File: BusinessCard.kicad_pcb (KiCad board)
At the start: 2 copper layers, 85.6 x 56 mm, 7 parts, among them U1 NT3H2111W0FHKH

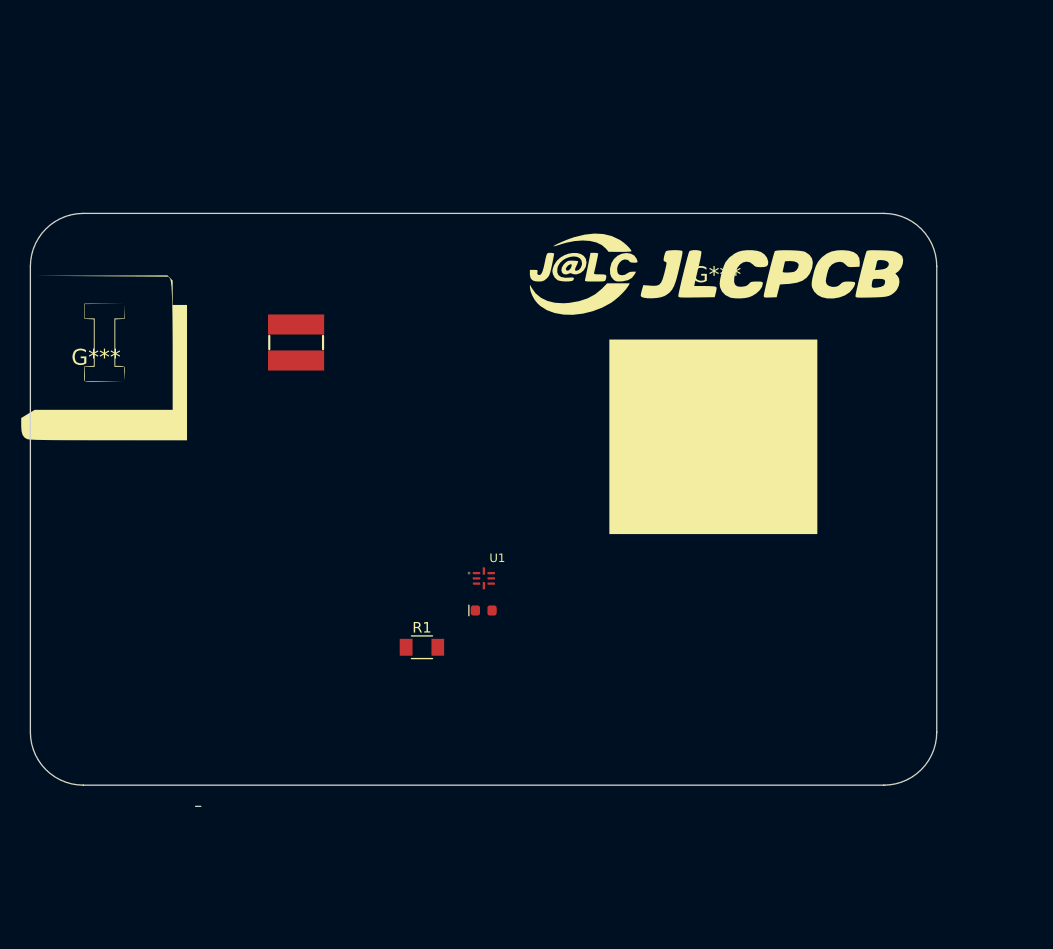
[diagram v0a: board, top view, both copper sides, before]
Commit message: logos added to footprint
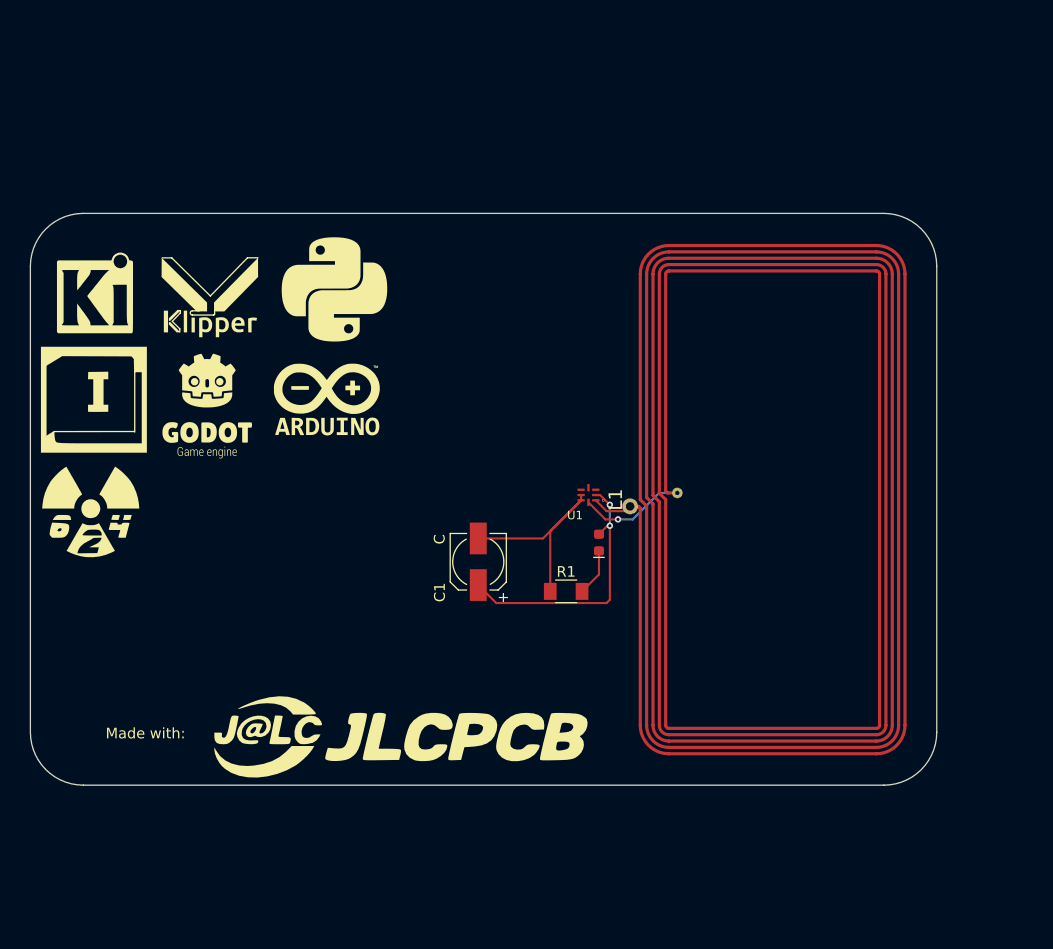
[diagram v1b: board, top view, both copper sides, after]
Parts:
- removed the G*** at (138.4, 87.1)
- added C1: C, PCM_4ms_Capacitor:CP_Elec_5x5.3, F.Cu at (116.2, 98.9)
- added G***: LOGO, nfc:klipper, F.Cu at (90.9, 73.8)
- added G***: LOGO, nfc:python, F.Cu at (102.6, 73.1)
- added G***: LOGO, nfc:624Logo, F.Cu at (79.6, 94.2)
- added G***: LOGO, nfc:arduino, F.Cu at (101.9, 83.6)
- added G***: LOGO, nfc:Kicad, F.Cu at (80.0, 73.6)
- added G***: LOGO, nfc:godot, F.Cu at (90.6, 84.2)
- L1: footprint PCM_SparkFun-Coil:Inductor_4.7x4.7mm -> nfc:25X48MM_NFC_ANTENNA
- moved G*** 52.9 mm to (108.9, 115.5)
- moved L1 47.4 mm to (144.0, 93.0), turned to 90 degrees
- moved R1 14.6 mm to (124.5, 101.7)
- moved D1 12.6 mm to (127.6, 97.1), turned to 90 degrees
- moved U1 12.6 mm to (126.6, 92.6), turned to 180 degrees
- moved G*** 4.00 mm to (79.9, 83.6)
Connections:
- D1 pad 2: Net-(D1-A) -> Net-(C1-+)
- R1 pad 1: Net-(U1-VSS) -> Net-(C1--)
- R1 pad 2: Net-(D1-A) -> Net-(D1-K)
- U1 pad 2: Net-(U1-VSS) -> Net-(C1-+)
- U1 pad 6: unconnected-(U1-VCC-Pad6) -> Net-(C1--)
- U1 pad 7: Net-(D1-K) -> Net-(C1--)
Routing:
- net Net-(C1-+): track 0.00 -> 25.3 mm, vias 0 -> 2
- net Net-(C1--): track 0.00 -> 21.5 mm
- net Net-(U1-LB): track 0.00 -> 10.1 mm, vias 0 -> 1
- net Net-(D1-K): track 0.00 -> 4.49 mm
- net Net-(U1-LA): track 0.00 -> 3.66 mm
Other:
- board size 85.6 x 56 mm -> 85.6 x 54 mm
- board text added: "Made with:"

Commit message: new footprints, got the pads working
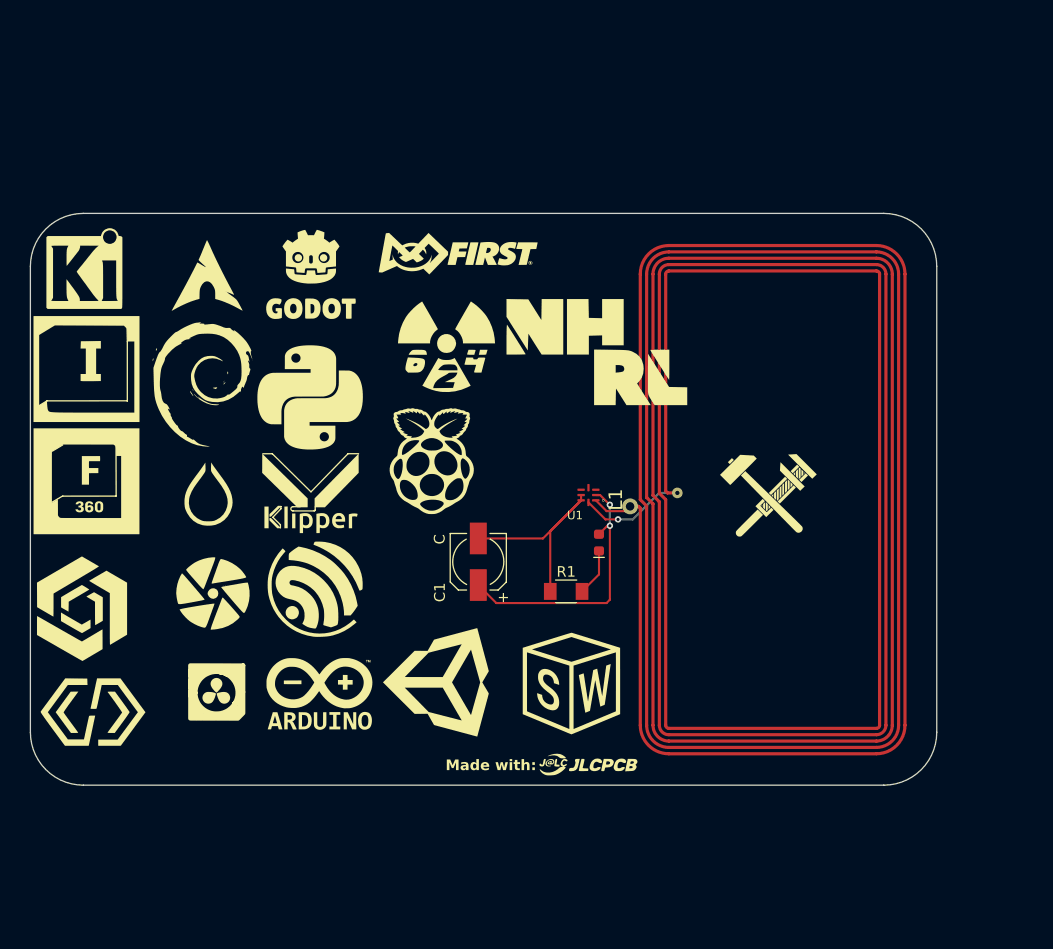
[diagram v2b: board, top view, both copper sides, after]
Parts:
- added G***: LOGO, nfc:raspberrypi, F.Cu at (111.8, 89.4)
- added G***: LOGO, nfc:onshape, F.Cu at (78.9, 103.4)
- added G***: LOGO, nfc:Solidworks, F.Cu at (125.0, 110.4)
- added G***: LOGO, nfc:Fusion360, F.Cu at (79.2, 91.3)
- added G***: LOGO, nfc:ESP, F.Cu at (100.8, 101.5)
- added G***: LOGO, nfc:Arch, F.Cu at (90.6, 72.7)
- added G***: LOGO, nfc:Unity, F.Cu at (112.2, 110.3)
- added G***: LOGO, nfc:DavinciResolve, F.Cu at (94.0, 111.2)
- added G***: LOGO, nfc:DarkTable, F.Cu at (103.1, 101.9)
- added G***: LOGO, nfc:hammerAndSpanner, F.Cu at (143.6, 92.7)
- added G***: LOGO, nfc:FRC, F.Cu at (114.3, 69.8)
- added G***: LOGO, nfc:moon, B.Cu at (90.4, 72.8)
- added G***: LOGO, nfc:WPIlib, F.Cu at (79.8, 113.0)
- added G***: LOGO, nfc:hyprland, F.Cu at (90.7, 92.5)
- added G***: LOGO, nfc:NHRL, F.Cu at (127.4, 79.1)
- added G***: LOGO, nfc:Debian, F.Cu at (90.2, 82.1)
- moved G*** 37.0 mm to (113.2, 78.6)
- moved G*** 27.8 mm to (101.2, 111.4)
- moved G*** 20.8 mm to (100.4, 92.3)
- moved G*** 17.9 mm to (126.6, 118.1)
- moved G*** 15.3 mm to (100.4, 72.5)
- moved G*** 10.5 mm to (100.3, 83.3)
- moved G*** 2.98 mm to (79.2, 80.7)
- moved G*** 2.51 mm to (79.0, 71.3)
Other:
- board text added: "JudasLilith"

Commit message: Made a few design changes, started the intro
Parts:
- added QR*****: https://github.com/JudasLilith, nfc:https___github.com_JudasLilith, B.Cu at (116.0, 74.8)
- C1: footprint PCM_4ms_Capacitor:CP_Elec_5x5.3 -> nfc:CAPC1608X90N
- D1: footprint PCM_SparkFun-LED:LED_0603_1608Metric -> nfc:LED0805-R-RD
- R1: footprint PCM_fab:R_1206 -> nfc:C0603
- moved G*** 62.0 mm to (141.3, 57.9), turned to 90 degrees
- moved G*** 59.0 mm to (94.0, 128.4), turned to 90 degrees
- moved G*** 57.8 mm to (135.7, 127.6), turned to 90 degrees
- moved G*** 53.5 mm to (126.1, 128.5), turned to 90 degrees
- moved G*** 53.3 mm to (103.4, 128.2), turned to 90 degrees
- moved G*** 50.7 mm to (114.0, 128.2), turned to 90 degrees
- moved G*** 44.3 mm to (95.4, 116.8), turned to 90 degrees
- moved L1 42.5 mm to (115.4, 61.7), turned to 180 degrees
- moved G*** 40.4 mm to (115.4, 63.8), turned to 90 degrees
- moved G*** 40.0 mm to (133.9, 113.4), turned to 90 degrees
- moved G*** 38.0 mm to (104.8, 117.2), turned to 90 degrees
- moved G*** 34.9 mm to (95.2, 107.0), turned to 90 degrees
- moved G*** 34.4 mm to (115.2, 116.7), turned to 90 degrees
- moved G*** 33.4 mm to (134.1, 106.2), turned to 90 degrees
- moved G*** 31.9 mm to (92.5, 93.1), turned to 90 degrees
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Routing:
- net Net-(C1--): track 21.5 -> 7.87 mm
- net Net-(C1-+): track 25.3 -> 19.7 mm, vias 2 -> 0
- net Net-(D1-K): track 4.49 -> 6.88 mm
- net Net-(U1-LB): track 10.1 -> 8.21 mm
- net Net-(U1-LA): track 3.66 -> 3.05 mm
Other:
- board size 85.6 x 54 mm -> 54 x 85.6 mm
- board text added: "+1(346)-287-4367"
- board text added: "-Beginner GameDev & WebDev"
- board text added: "-FRC,NTHS,TSA & Hack Club"
- board text added: "-Hobby CAD student"
- board text added: "-Hobby Mill and CNC machinist"
- board text added: "-PCB designer"
- board text added: "-Supreme™ Archlinux user"
- board text added: "He/him"
- board text added: "Judaslilith.com"
- board text added: "Slack ID: @JudasLilith"
- board text added: "judas1lilith@gmail.com"
- board text removed: "JudasLilith"

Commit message: Final push after ordering
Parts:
- removed the G*** at (115.4, 63.8)
- removed the G*** at (116.0, 91.3)
- removed the QR***** at (116.0, 74.8)
- added G***: LOGO, nfcactual:hackClub, F.Cu at (164.9, 60.9)
- added G***: LOGO, nfcactual:moon, B.Cu at (125.9, 82.4)
- added QR*****: https://github.com/JudasLilith, nfcactual:https___github.com_JudasLilith, B.Cu at (142.2, 82.5)
- moved G*** 62.0 mm to (97.9, 68.3), turned to 0 degrees
- moved G*** 56.2 mm to (90.2, 78.1), turned to 0 degrees
- moved G*** 52.3 mm to (158.5, 107.3), turned to 0 degrees
- moved G*** 50.3 mm to (88.0, 95.8), turned to 0 degrees
- moved G*** 47.6 mm to (125.2, 58.4), turned to 0 degrees
- moved G*** 44.9 mm to (108.5, 91.9), turned to 0 degrees
- moved L1 44.0 mm to (154.7, 81.4), turned to 90 degrees
- moved G*** 42.7 mm to (87.6, 86.1), turned to 0 degrees
- moved G*** 40.2 mm to (119.0, 66.8), turned to 0 degrees
- moved G*** 38.7 mm to (108.8, 68.5), turned to 0 degrees
- moved G*** 38.4 mm to (87.8, 69.3), turned to 0 degrees
- moved G*** 37.1 mm to (98.3, 96.7), turned to 0 degrees
- moved G*** 36.8 mm to (108.3, 80.5), turned to 0 degrees
- moved G*** 34.7 mm to (128.5, 102.2), turned to 0 degrees
- moved G*** 32.7 mm to (129.1, 76.9), turned to 0 degrees
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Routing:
- net Net-(C1--): track 7.87 -> 10.1 mm
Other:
- board size 54 x 85.6 mm -> 85.6 x 54 mm
- board text added: "& more"
- board text added: "-CAD student/PCB designerr"
- board text added: "FRC,NTHS,"
- board text added: "TSA, Hack Clubr r"
- board text added: "Tap Me!"
- board text added: "Things I've used/ Interested in:"
- board text removed: "-FRC,NTHS,TSA & Hack Club"
- board text removed: "-Hobby CAD student"
- board text removed: "-PCB designer"

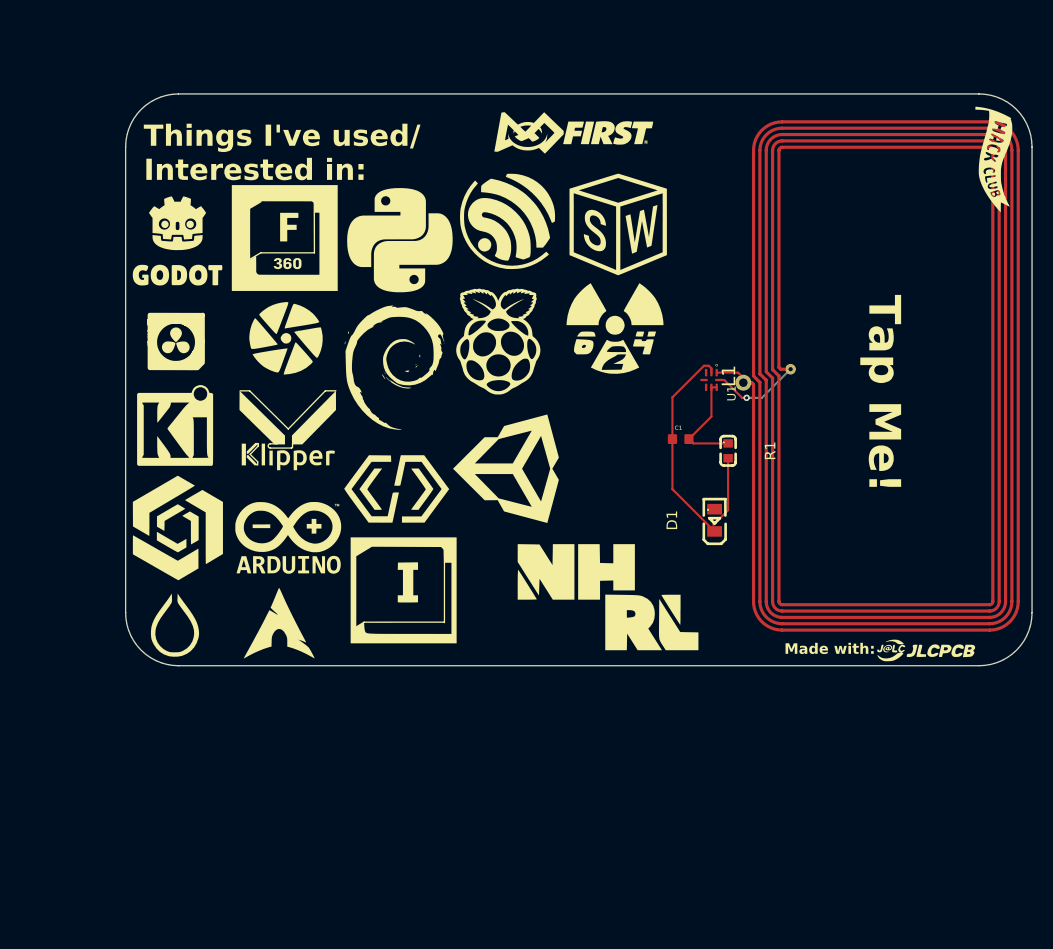
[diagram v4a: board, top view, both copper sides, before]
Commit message: A sub-project where I make a business card for a company I'm working for
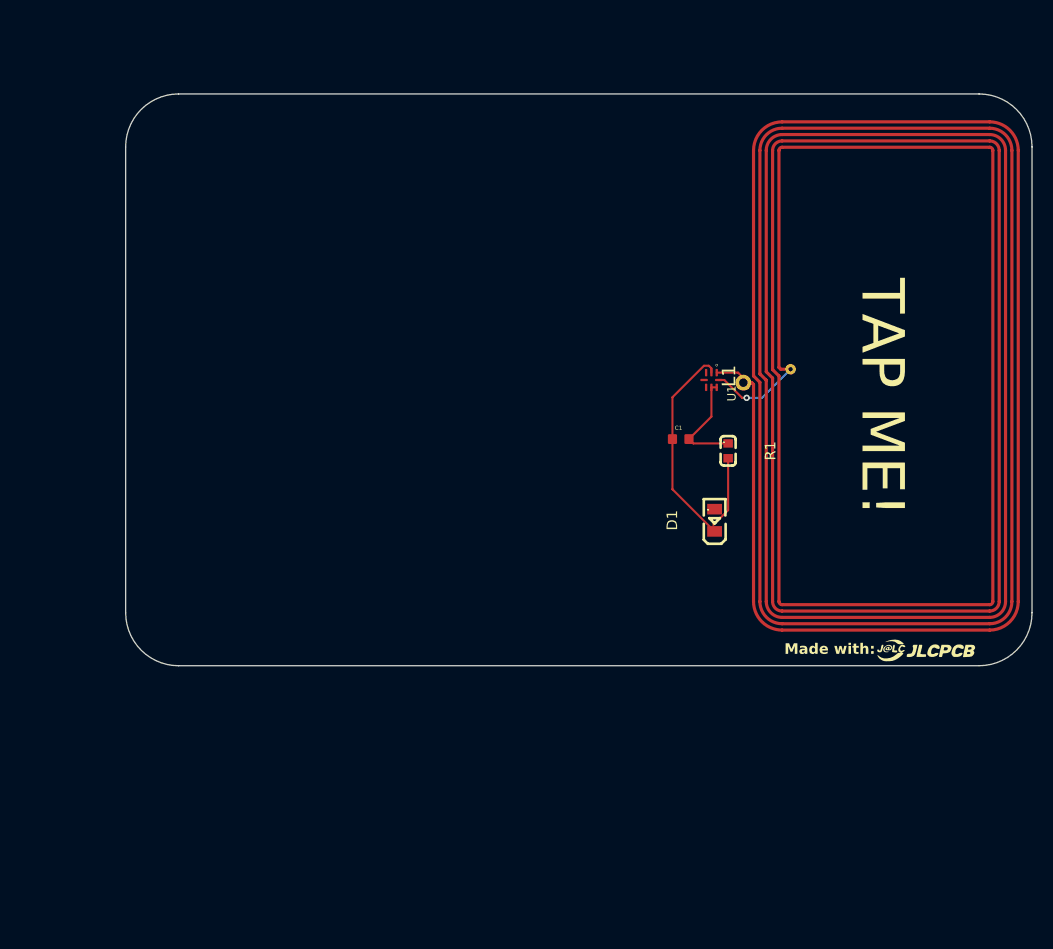
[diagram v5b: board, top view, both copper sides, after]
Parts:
- removed the G*** at (118.1, 78.1)
- removed the G*** at (129.1, 76.9)
- removed the G*** at (98.3, 96.7)
- removed the G*** at (88.0, 95.8)
- removed the G*** at (129.4, 67.0)
- removed the G*** at (97.9, 68.3)
- removed the G*** at (87.6, 86.1)
- removed the G*** at (119.0, 66.8)
- removed the G*** at (97.4, 105.5)
- removed the G*** at (118.8, 90.1)
- removed the G*** at (90.2, 78.1)
- removed the G*** at (110.0, 77.8)
- removed the G*** at (164.9, 60.9)
- removed the G*** at (125.2, 58.4)
- removed the G*** at (87.8, 69.3)
- removed the G*** at (125.9, 82.4)
- removed the G*** at (108.5, 91.9)
- removed the G*** at (98.3, 86.4)
- removed the G*** at (109.2, 101.6)
- removed the G*** at (108.8, 68.5)
- removed the G*** at (87.5, 104.9)
- removed the G*** at (128.5, 102.2)
- removed the G*** at (108.3, 80.5)
- removed QR*****: https://github.com/JudasLilith, nfcactual:https___github.com_JudasLilith
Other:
- board text added: "23915 Bonnamere Ln. Katy, Texas, 77494"
- board text added: "Capt. Connor(Baikseok) Seo"
- board text added: "Mobile) +1 713-206-7744"
- board text added: "Phone) +1 281-665-8655"
- board text added: "TAP ME!"
- board text added: "Whitestone Marine Corp."
- board text added: "connor.seo@whitestone21.com"
- board text removed: "& more"
- board text removed: "+1(346)-287-4367"
- board text removed: "-Beginner GameDev & WebDev"
- board text removed: "-CAD student/PCB designerr"
- board text removed: "-Hobby Mill and CNC machinist"
- board text removed: "-Supreme™ Archlinux user"
- board text removed: "FRC,NTHS,"
- board text removed: "He/him"
- board text removed: "Judaslilith.com"
- board text removed: "Slack ID: @JudasLilith"
- board text removed: "TSA, Hack Clubr r"
- board text removed: "Tap Me!"
- board text removed: "Things I've used/ Interested in:"
- board text removed: "judas1lilith@gmail.com"

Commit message: made a new card on a new branch for a company(custom job)
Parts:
- added G***: LOGO, nfcactual:co, B.Cu at (99.0, 86.0)
